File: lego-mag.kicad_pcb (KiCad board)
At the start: 2 copper layers, 57.2 x 52.1 mm, 29 parts, among them IC1 4N35, P1 CONN_1, P2 CONN_1, P3 CONN_2, P5 CONN_1, P6 CONN_1, Q1 NPN

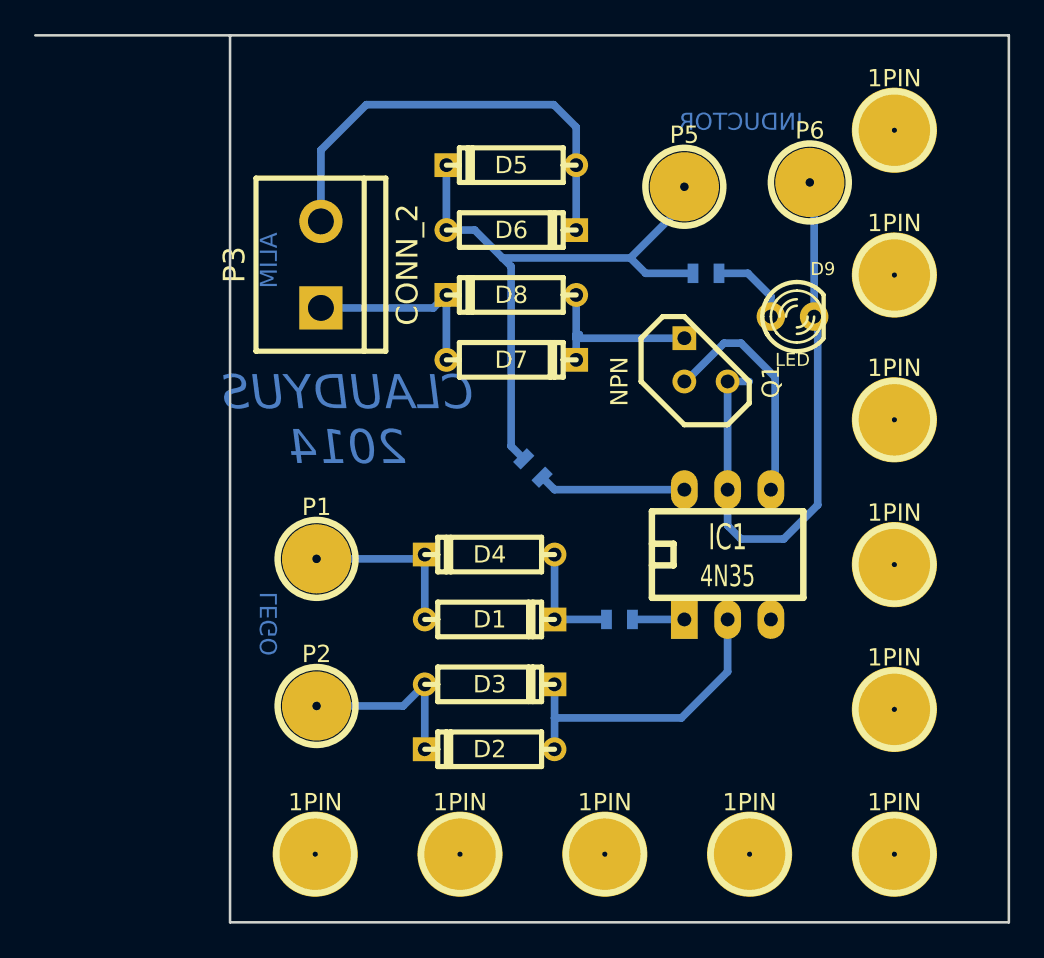
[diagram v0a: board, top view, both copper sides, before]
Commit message: Update to v1 with correct diode connection
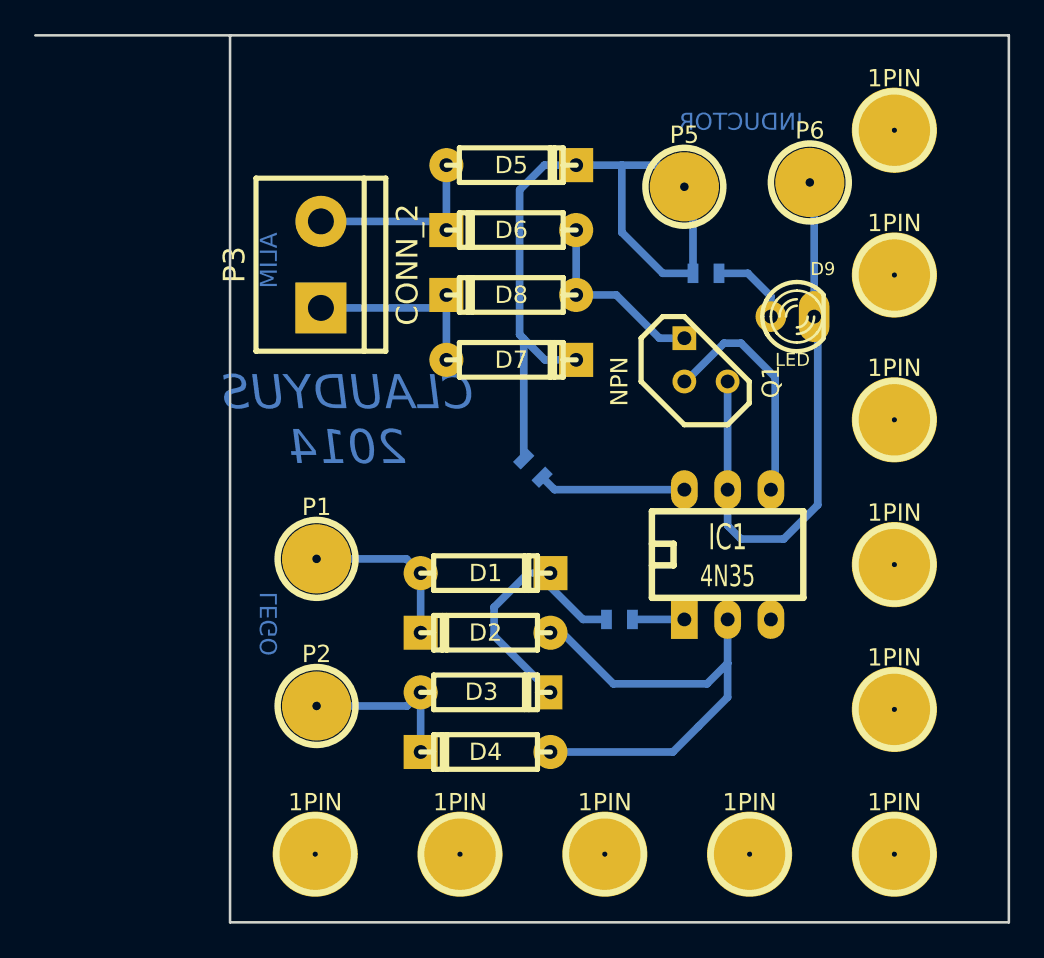
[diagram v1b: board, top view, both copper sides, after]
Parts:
- moved D4 11.6 mm to (169.9, 134.8)
- moved D2 6.84 mm to (169.9, 127.8)
- moved D1 2.73 mm to (169.9, 124.3)
- moved D3 0.53 mm to (169.9, 131.3)
- turned D5 to 0 degrees
- turned D6 to 180 degrees
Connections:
- D1 pad 1: N-0000016 -> N-0000014
- D1 pad 2: N-0000013 (its old number) -> N-0000015
- D2 pad 1: N-0000014 -> N-0000012
- D2 pad 2: N-0000017 -> N-0000014
- D3 pad 1: N-0000017 -> N-000001
- D3 pad 2: N-0000014 -> N-0000015
- D4 pad 1: N-0000013 (its old number) -> N-0000012
- D4 pad 2: N-0000016 -> N-000001
- D5 pad 2: N-0000012 -> N-0000011
- D6 pad 1: N-0000012 -> GND
- D7 pad 2: GND -> N-0000011
- IC1 pad 2: N-0000014 -> N-0000012
- P1 pad 1: N-0000016 -> N-0000014
- P2 pad 1: N-0000017 -> N-000001
- P5 pad 1: N-0000012 -> N-0000011
- R1 pad 1: N-0000013 (its old number) -> N-0000015
- R2 pad 2: N-0000012 -> N-0000011
- R3 pad 2: N-0000012 -> N-0000011
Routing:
- net N-0000011: track 0.00 -> 45.0 mm
- net N-000008: track 26.9 -> 11.4 mm
- net N-0000015: track 0.00 -> 15.4 mm
- net N-0000017: track 10.7 -> 0.00 mm
- net N-0000016: track 10.3 -> 0.00 mm
- net N-000001: track 0.00 -> 9.94 mm
- net N-0000012: track 37.1 -> 28.4 mm
- net N-0000014: track 18.2 -> 9.96 mm
- net N-0000013 (its old number): track 6.86 -> 0.00 mm
- net N-000004: track 35.3 -> 34.0 mm
- net GND: track 10.6 -> 11.2 mm
